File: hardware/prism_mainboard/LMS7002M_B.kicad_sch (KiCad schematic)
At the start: 1 part, among them U2 LMS7002M

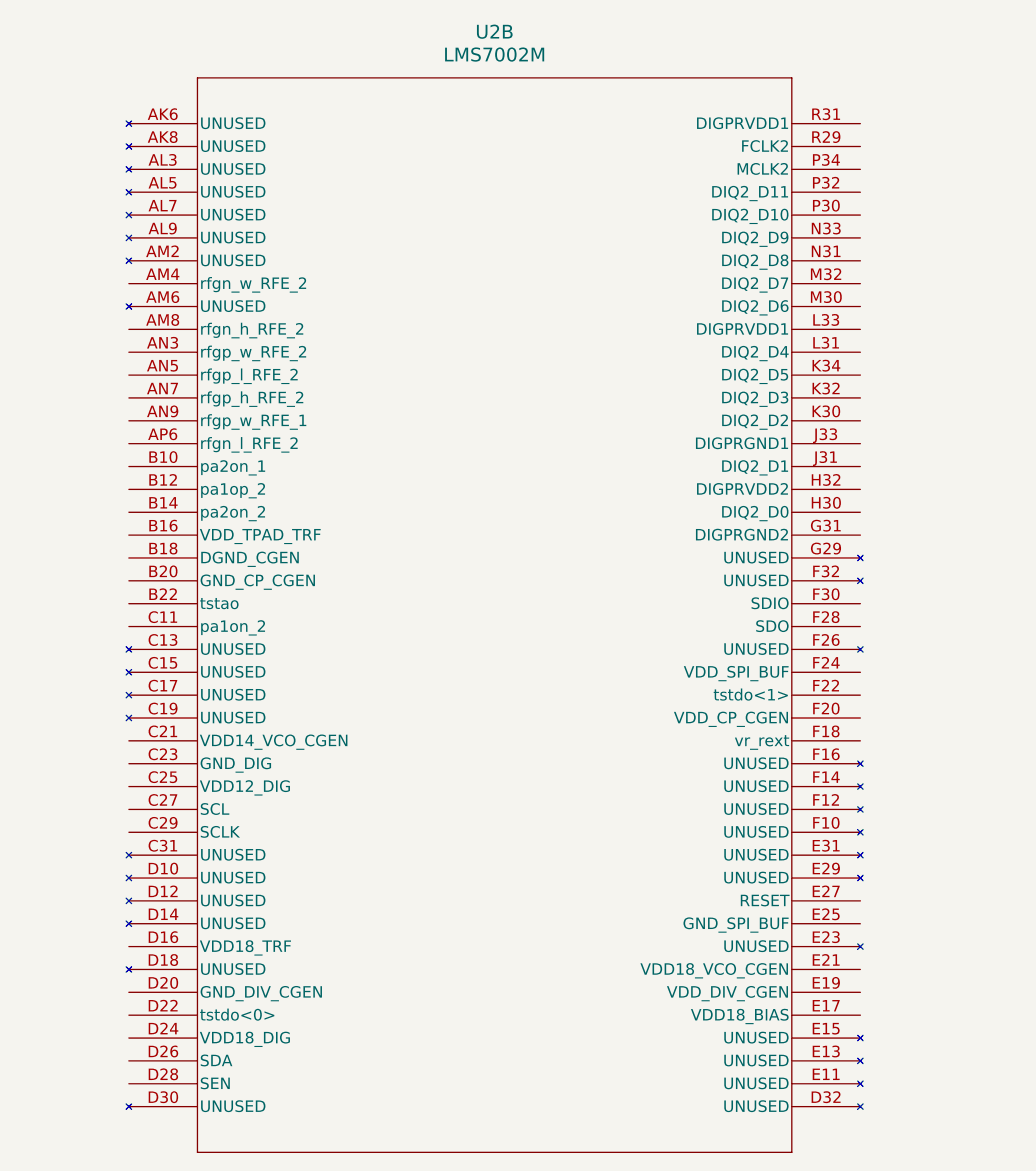
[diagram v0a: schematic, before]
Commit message: Mainboard Updates
Started a lot of the basic schematic nets like GND and Power nets. Major Change: Decided on using the XC7Z015-1CLG485I instead of the 7010 or 7020 due to the ability to use HDMI interfaces with an adapter and more LUTs. Updated schematic symbols and footprints accordingly. Added Memory, Encoder, MicroSD schematics. Added LimeSDR footprints as well. Will Try to add Power to the entire board next.
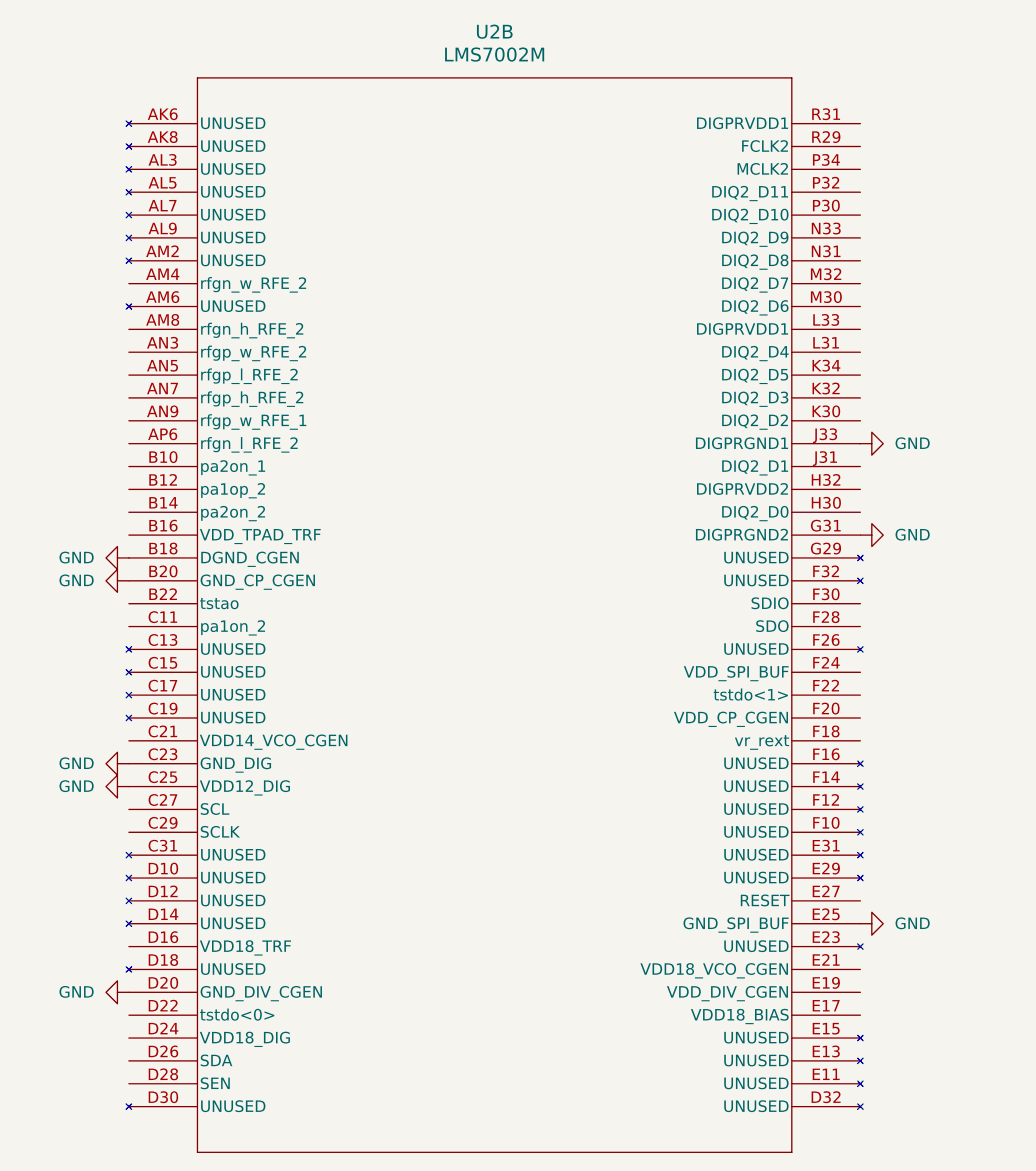
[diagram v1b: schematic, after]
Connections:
- net GND: now reaches U2.B18 (DGND_CGEN)
- net GND: now also U2.B20 (GND_CP_CGEN), U2.C23 (GND_DIG), U2.C25 (VDD12_DIG), U2.D20 (GND_DIV_CGEN), U2.E25 (GND_SPI_BUF), U2.G31 (DIGPRGND2), U2.J33 (DIGPRGND1)

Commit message: Schematic Updates
Updated schematics. Most of the power and decoupling is set for most if not all devices. Need to interconnect devices. Still reading datasheets
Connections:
- net VDD_1V8: now reaches U2.D16 (VDD18_TRF)
- net VDD_1V8: now also U2.D24 (VDD18_DIG), U2.E17 (VDD18_BIAS), U2.E21 (VDD18_VCO_CGEN)
- net VDD_1V8_DIG: now reaches U2.H32 (DIGPRVDD2)
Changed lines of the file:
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@@
 	(generator_version "10.0")
 	(paper "A4")
+	(global_label "VDD_1V8"
+		(shape input)
+		(at 104.14 142.24 180)
+		(fields_autoplaced yes)
+		(effects
+			(font
+				(size 1.27 1.27)
+			)
+			(justify right)
+		)
+		(property "Intersheetrefs" "${INTERSHEET_REFS}"
+			(at 93.051 142.24 0)
+			(hide yes)
+			(show_name no)
+			(do_not_autoplace no)
+			(effects
+				(font
+					(size 1.27 1.27)
+				)
+				(justify right)
+			)
+		)
+	)
+	(global_label "VDD_1V8_DIG"
+		(shape input)
+		(at 185.42 81.28 0)
+		(fields_autoplaced yes)
+		(effects
+			(font
+				(size 1.27 1.27)
+			)
+			(justify left)
+		)
+		(property "Intersheetrefs" "${INTERSHEET_REFS}"
+			(at 200.6214 81.28 0)
+			(hide yes)
+			(show_name no)
+			(do_not_autoplace no)
+			(effects
+				(font
+					(size 1.27 1.27)
+				)
+				(justify left)
+			)
+		)
+	)
+	(global_label "VDD_1V8"
+		(shape input)
+		(at 104.14 132.08 180)
+		(fields_autoplaced yes)
+		(effects
+			(font
+				(size 1.27 1.27)
+			)
+			(justify right)
+		)
+		(property "Intersheetrefs" "${INTERSHEET_REFS}"
+			(at 93.051 132.08 0)
+			(hide yes)
+			(show_name no)
+			(do_not_autoplace no)
+			(effects
+				(font
+					(size 1.27 1.27)
+				)
+				(justify right)
+			)
+		)
+	)
+	(global_label "VDD_1V8"
+		(shape input)
+		(at 185.42 134.62 0)
+		(fields_autoplaced yes)
+		(effects
+			(font
+				(size 1.27 1.27)
+			)
+			(justify left)
+		)
+		(property "Intersheetrefs" "${INTERSHEET_REFS}"
+			(at 196.509 134.62 0)
+			(hide yes)
+			(show_name no)
+			(do_not_autoplace no)
+			(effects
+				(font
+					(size 1.27 1.27)
+				)
+				(justify left)
+			)
+		)
+	)
+	(global_label "VDD_1V8"
+		(shape input)
+		(at 185.42 139.7 0)
+		(fields_autoplaced yes)
+		(effects
+			(font
+				(size 1.27 1.27)
+			)
+			(justify left)
+		)
+		(property "Intersheetrefs" "${INTERSHEET_REFS}"
+			(at 196.509 139.7 0)
+			(hide yes)
+			(show_name no)
+			(do_not_autoplace no)
+			(effects
+				(font
+					(size 1.27 1.27)
+				)
+				(justify left)
+			)
+		)
+	)
 	(symbol
 		(lib_id "power:GND")

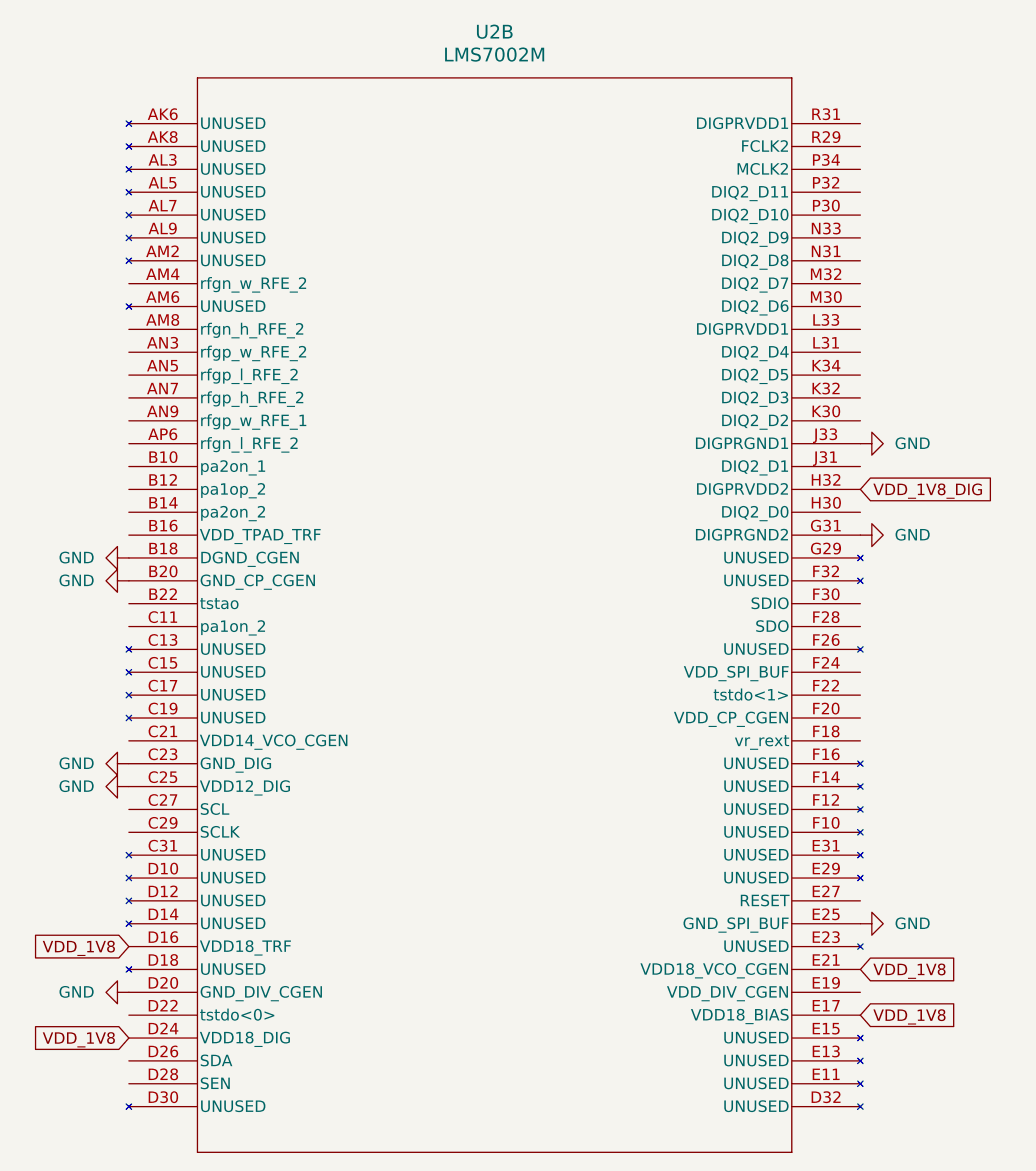
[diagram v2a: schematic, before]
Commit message: Schematic Updates
Added the LMS7002M to XC7Z015 connections, atleast the preliminary data connections.
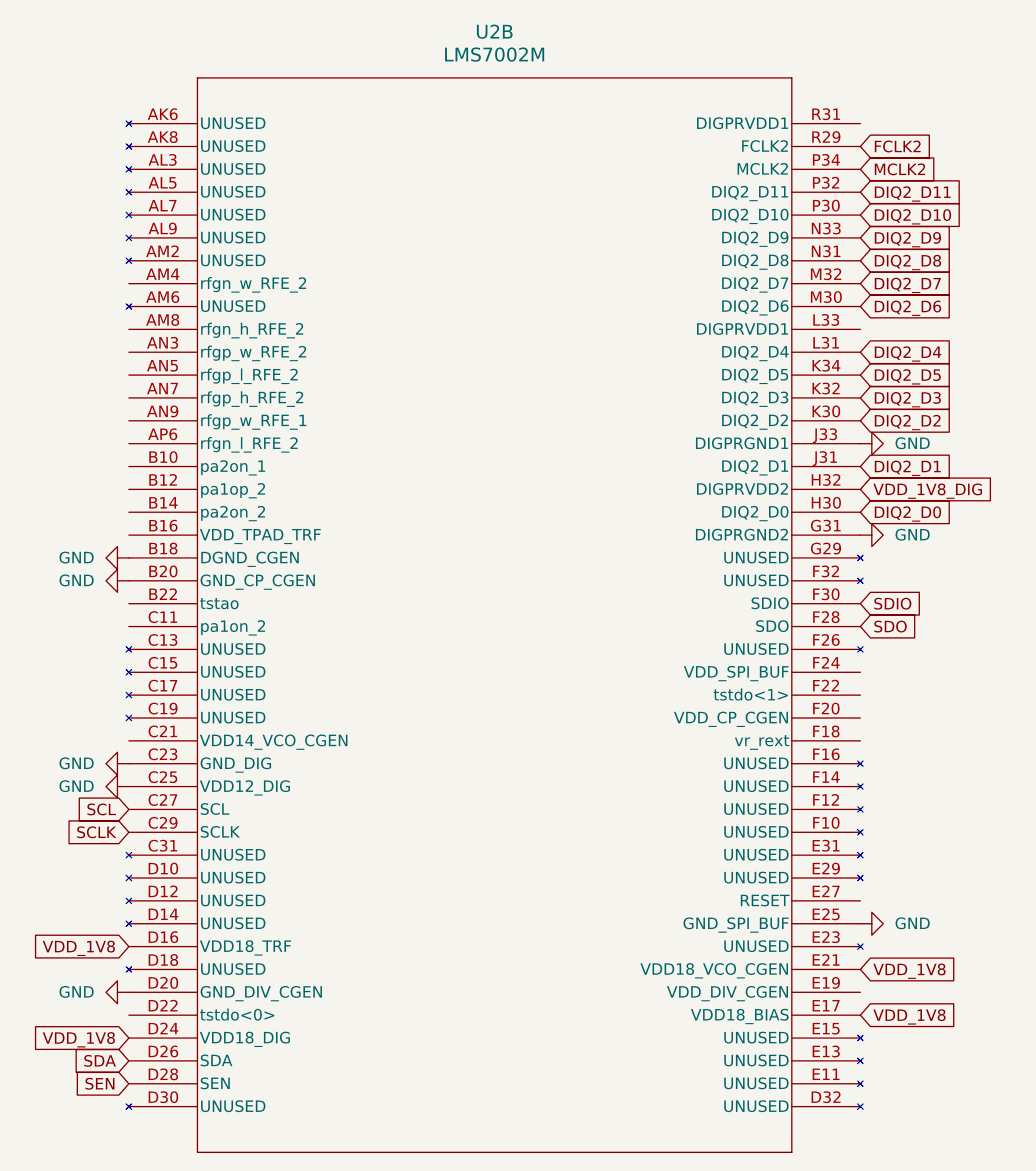
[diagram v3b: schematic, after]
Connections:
- net SCL: now reaches U2.C27 (SCL)
- net SCLK: now reaches U2.C29 (SCLK)
- net SDA: now reaches U2.D26 (SDA)
- net SEN: now reaches U2.D28 (SEN)
- net SDO: now reaches U2.F28 (SDO)
- net SDIO: now reaches U2.F30 (SDIO)
- net DIQ2_D0: now reaches U2.H30 (DIQ2_D0)
- net DIQ2_D1: now reaches U2.J31 (DIQ2_D1)
- net DIQ2_D2: now reaches U2.K30 (DIQ2_D2)
- net DIQ2_D3: now reaches U2.K32 (DIQ2_D3)
- net DIQ2_D5: now reaches U2.K34 (DIQ2_D5)
- net DIQ2_D4: now reaches U2.L31 (DIQ2_D4)
- net DIQ2_D6: now reaches U2.M30 (DIQ2_D6)
- net DIQ2_D7: now reaches U2.M32 (DIQ2_D7)
- net DIQ2_D8: now reaches U2.N31 (DIQ2_D8)
- net DIQ2_D9: now reaches U2.N33 (DIQ2_D9)
- net DIQ2_D10: now reaches U2.P30 (DIQ2_D10)
- net DIQ2_D11: now reaches U2.P32 (DIQ2_D11)
- net MCLK2: now reaches U2.P34 (MCLK2)
- net FCLK2: now reaches U2.R29 (FCLK2)

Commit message: Updates
Mostly Schematic updates, nothing too big. Added a few datasheets
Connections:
- net LM_RST: now reaches U2.E27 (RESET)
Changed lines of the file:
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@@
+		)
+	)
+	(global_label "LM_RST"
+		(shape input)
+		(at 185.42 127 0)
+		(fields_autoplaced yes)
+		(effects
+			(font
+				(size 1.27 1.27)
+			)
+			(justify left)
+		)
+		(property "Intersheetrefs" "${INTERSHEET_REFS}"
+			(at 195.2994 127 0)
+			(hide yes)
+			(show_name no)
+			(do_not_autoplace no)
+			(effects
+				(font
+					(size 1.27 1.27)
+				)
+				(justify left)
+			)
 		)
 	)
